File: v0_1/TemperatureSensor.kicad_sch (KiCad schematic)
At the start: 1 part, among them U3 AHT20

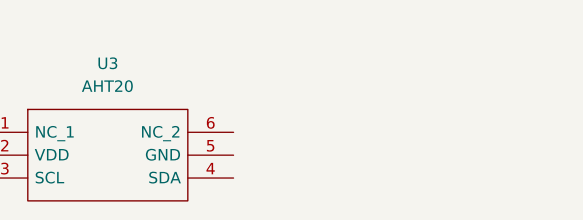
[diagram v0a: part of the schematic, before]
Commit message: add battery case
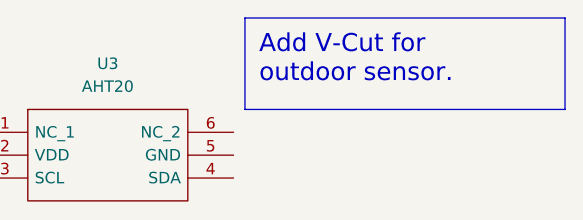
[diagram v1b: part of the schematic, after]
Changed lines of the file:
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@@
 (kicad_sch (version 20230121) (generator eeschema)
   (paper "A4")
+  (text_box "Add V-Cut for outdoor sensor.\n"
+    (at 128.27 67.31 0) (size 35.56 10.16)
+    (stroke (width 0) (type default))
+    (fill (type color) (color 235 255 31 1))
+    (effects (font (size 2 2)) (justify left top))
+  )
   (symbol (lib_id "AHT20:AHT20") (at 99.06 80.01 0) (unit 1)
     (in_bom yes) (on_board yes) (dnp no) (fields_autoplaced)

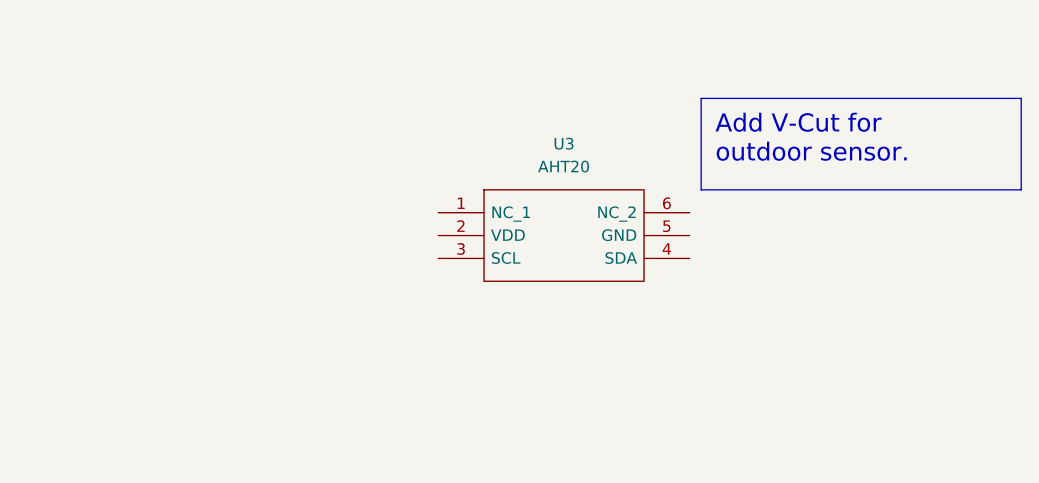
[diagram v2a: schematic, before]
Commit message: add rtc and charger schematic
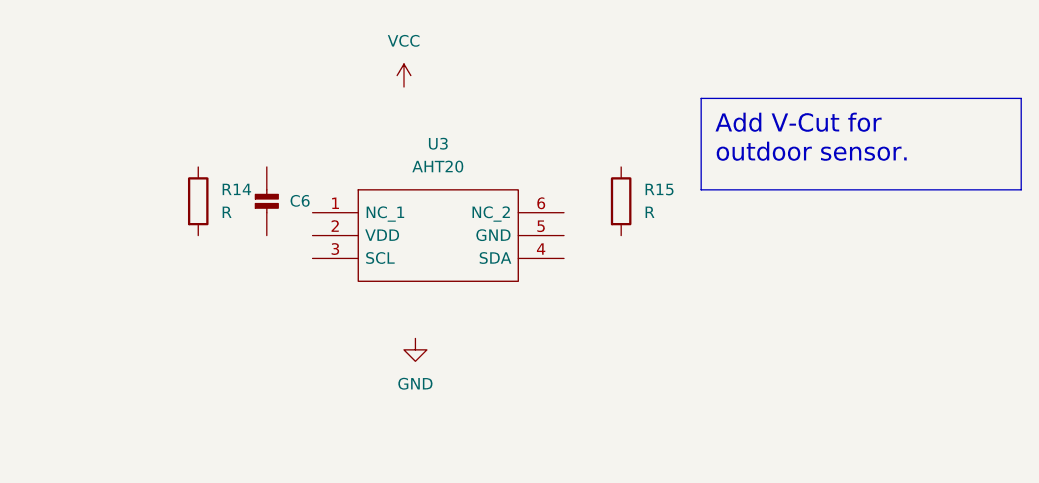
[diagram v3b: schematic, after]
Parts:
- added C6: ~, v0_1:_0603, symbol v0_1-eagle-import:CAP_CERAMIC_0603
- added R14, R15: R, symbol Device:R
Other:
- moved on the sheet: U3
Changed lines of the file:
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@@
     (effects (font (size 2 2)) (justify left top))
   )
-  (symbol (lib_id "AHT20:AHT20") (at 99.06 80.01 0) (unit 1)
+  (symbol (lib_id "AHT20:AHT20") (at 85.09 80.01 0) (unit 1)
     (in_bom yes) (on_board yes) (dnp no) (fields_autoplaced)
-    (property "Reference" "U3" (at 113.03 72.39 0)
+    (property "Reference" "U3" (at 99.06 72.39 0)
       (effects (font (size 1.27 1.27)))
     )
-    (property "Value" "AHT20" (at 113.03 74.93 0)
+    (property "Value" "AHT20" (at 99.06 74.93 0)
       (effects (font (size 1.27 1.27)))
     )
-    (property "Footprint" "AHT20:AHT20" (at 123.19 77.47 0)
+    (property "Footprint" "AHT20:AHT20" (at 109.22 77.47 0)
       (effects (font (size 1.27 1.27)) (justify left) hide)
     )
-    (property "Datasheet" "http://www.aosong.com/userfiles/files/media/Data%20Sheet%20AHT20.pdf" (at 123.19 80.01 0)
+    (property "Datasheet" "http://www.aosong.com/userfiles/files/media/Data%20Sheet%20AHT20.pdf" (at 109.22 80.01 0)
       (effects (font (size 1.27 1.27)) (justify left) hide)
     )
-    (property "Description" "Integrated temperature and humidity Sensor DC : 2.2 - 5.5V, 0 ~{} 100% RH, -40 ~{} + 85 ." (at 123.19 82.55 0)
+    (property "Description" "Integrated temperature and humidity Sensor DC : 2.2 - 5.5V, 0 ~{} 100% RH, -40 ~{} + 85 ." (at 109.22 82.55 0)
       (effects (font (size 1.27 1.27)) (justify left) hide)
     )
-    (property "Height" "1.1" (at 123.19 85.09 0)
+    (property "Height" "1.1" (at 109.22 85.09 0)
       (effects (font (size 1.27 1.27)) (justify left) hide)
     )
-    (property "Manufacturer_Name" "Aosong" (at 123.19 87.63 0)
+    (property "Manufacturer_Name" "Aosong" (at 109.22 87.63 0)
       (effects (font (size 1.27 1.27)) (justify left) hide)
     )
-    (property "Manufacturer_Part_Number" "AHT20" (at 123.19 90.17 0)
+    (property "Manufacturer_Part_Number" "AHT20" (at 109.22 90.17 0)
       (effects (font (size 1.27 1.27)) (justify left) hide)
     )
-    (property "Mouser Part Number" "" (at 123.19 92.71 0)
+    (property "Mouser Part Number" "" (at 109.22 92.71 0)
       (effects (font (size 1.27 1.27)) (justify left) hide)
     )
-    (property "Mouser Price/Stock" "" (at 123.19 95.25 0)
+    (property "Mouser Price/Stock" "" (at 109.22 95.25 0)
       (effects (font (size 1.27 1.27)) (justify left) hide)
     )
-    (property "Arrow Part Number" "" (at 123.19 97.79 0)
+    (property "Arrow Part Number" "" (at 109.22 97.79 0)
       (effects (font (size 1.27 1.27)) (justify left) hide)
     )
-    (property "Arrow Price/Stock" "" (at 123.19 100.33 0)
+    (property "Arrow Price/Stock" "" (at 109.22 100.33 0)
       (effects (font (size 1.27 1.27)) (justify left) hide)
     )
@@
         )
       )
+    )
+  )
+  (symbol (lib_id "power:GND") (at 96.52 93.98 0) (unit 1)
+    (in_bom yes) (on_board yes) (dnp no) (fields_autoplaced)
+    (property "Reference" "#PWR010" (at 96.52 100.33 0)
+      (effects (font (size 1.27 1.27)) hide)
+    )
+    (property "Value" "GND" (at 96.52 99.06 0)
+      (effects (font (size 1.27 1.27)))
+    )
+    (property "Footprint" "" (at 96.52 93.98 0)
+      (effects (font (size 1.27 1.27)) hide)
+    )
+    (property "Datasheet" "" (at 96.52 93.98 0)
+      (effects (font (size 1.27 1.27)) hide)
+    )
+    (pin "1")
+    (instances
+      (project "v0_1"
+        (path "/0bf090f4-b9b7-437f-9e6a-e818f47752ec/18c6dee4-287a-4eaf-8042-b3dc1f680c7d"
+          (reference "#PWR010") (unit 1)
+        )
+      )
+    )
+  )
+  (symbol (lib_id "power:VCC") (at 95.25 66.04 0) (unit 1)
+    (in_bom yes) (on_board yes) (dnp no) (fields_autoplaced)
+    (property "Reference" "#PWR09" (at 95.25 69.85 0)
+      (effects (font (size 1.27 1.27)) hide)
+    )
+    (property "Value" "VCC" (at 95.25 60.96 0)
+      (effects (font (size 1.27 1.27)))
+    )
+    (property "Footprint" "" (at 95.25 66.04 0)
+      (effects (font (size 1.27 1.27)) hide)
+    )
+    (property "Datasheet" "" (at 95.25 66.04 0)
+      (effects (font (size 1.27 1.27)) hide)
+    )
+    (pin "1")
+    (instances
+      (project "v0_1"
+        (path "/0bf090f4-b9b7-437f-9e6a-e818f47752ec/18c6dee4-287a-4eaf-8042-b3dc1f680c7d"
+          (reference "#PWR09") (unit 1)
+        )
+      )
+    )
+  )
+  (symbol (lib_id "v0_1-eagle-import:CAP_CERAMIC_0603") (at 80.01 80.01 0) (unit 1)
+    (in_bom yes) (on_board yes) (dnp no) (fields_autoplaced)
+    (property "Reference" "C6" (at 82.55 78.74 0)
+      (effects (font (size 1.27 1.27)) (justify left))
+    )
+    (property "Value" "~" (at 82.31 78.76 90)
+      (effects (font (size 1.27 1.27)))
+    )
+    (property "Footprint" "v0_1:_0603" (at 80.01 80.01 0)
+      (effects (font (size 1.27 1.27)) hide)
+    )
+    (property "Datasheet" "" (at 80.01 80.01 0)
+      (effects (font (size 1.27 1.27)) hide)
+    )
+    (pin "1")
+    (pin "2")
+    (instances
+      (project "v0_1"
+        (path "/0bf090f4-b9b7-437f-9e6a-e818f47752ec/18c6dee4-287a-4eaf-8042-b3dc1f680c7d"
+          (reference "C6") (unit 1)
+        )
+      )
+    )
+  )
+  (symbol (lib_id "Device:R") (at 119.38 78.74 0) (unit 1)
+    (in_bom yes) (on_board yes) (dnp no) (fields_autoplaced)
+    (property "Reference" "R15" (at 121.92 77.47 0)
+      (effects (font (size 1.27 1.27)) (justify left))
+    )
+    (property "Value" "R" (at 121.92 80.01 0)
+      (effects (font (size 1.27 1.27)) (justify left))
+    )
+    (property "Footprint" "" (at 117.602 78.74 90)
+      (effects (font (size 1.27 1.27)) hide)
+    )
+    (property "Datasheet" "~" (at 119.38 78.74 0)
+      (effects (font (size 1.27 1.27)) hide)
+    )
+    (pin "1")
+    (pin "2")
+    (instances
+      (project "v0_1"
+        (path "/0bf090f4-b9b7-437f-9e6a-e818f47752ec/18c6dee4-287a-4eaf-8042-b3dc1f680c7d"
+          (reference "R15") (unit 1)
+        )
+      )
+    )
+  )
+  (symbol (lib_id "Device:R") (at 72.39 78.74 0) (unit 1)
+    (in_bom yes) (on_board yes) (dnp no) (fields_autoplaced)
+    (property "Reference" "R14" (at 74.93 77.47 0)
+      (effects (font (size 1.27 1.27)) (justify left))
+    )
+    (property "Value" "R" (at 74.93 80.01 0)
+      (effects (font (size 1.27 1.27)) (justify left))
+    )
+    (property "Footprint" "" (at 70.612 78.74 90)
+      (effects (font (size 1.27 1.27)) hide)
+    )
+    (property "Datasheet" "~" (at 72.39 78.74 0)
+      (effects (font (size 1.27 1.27)) hide)
+    )
+    (pin "1")
+    (pin "2")
+    (instances
+      (project "v0_1"
+        (path "/0bf090f4-b9b7-437f-9e6a-e818f47752ec/18c6dee4-287a-4eaf-8042-b3dc1f680c7d"
+          (reference "R14") (unit 1)
+        )
+      )

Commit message: add 0.2V
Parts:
- C6: value ~ -> 10uF
- R14, R15: value R -> 10K
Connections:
- net GND: now also C6.2, U3.5 (GND)
- net +3.3V: now reaches U3.2 (VDD)
- net +3.3V: now also C6.1, R14.1, R15.1
- net SCL: now reaches U3.3 (SCL)
- net SCL: now also R14.2
- net SDA: now reaches U3.4 (SDA)
- net SDA: now also R15.2
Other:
- moved on the sheet: C6, R14, R15
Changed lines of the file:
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@@
 (kicad_sch (version 20230121) (generator eeschema)
   (paper "A4")
+  (junction (at 81.28 82.55) (diameter 0) (color 0 0 0 0)
+  )
+  (junction (at 76.2 67.31) (diameter 0) (color 0 0 0 0)
+  )
+  (junction (at 76.2 85.09) (diameter 0) (color 0 0 0 0)
+  )
+  (junction (at 68.58 88.9) (diameter 0) (color 0 0 0 0)
+  )
+  (junction (at 81.28 99.06) (diameter 0) (color 0 0 0 0)
+  )
+  (junction (at 68.58 67.31) (diameter 0) (color 0 0 0 0)
+  )
+  (wire (pts (xy 58.42 88.9) (xy 68.58 88.9))
+    (stroke (width 0) (type default))
+  )
+  (wire (pts (xy 76.2 67.31) (xy 81.28 67.31))
+    (stroke (width 0) (type default))
+  )
+  (wire (pts (xy 68.58 67.31) (xy 76.2 67.31))
+    (stroke (width 0) (type default))
+  )
+  (wire (pts (xy 81.28 82.55) (xy 81.28 67.31))
+    (stroke (width 0) (type default))
+  )
+  (wire (pts (xy 58.42 85.09) (xy 76.2 85.09))
+    (stroke (width 0) (type default))
+  )
+  (wire (pts (xy 113.03 82.55) (xy 116.84 82.55))
+    (stroke (width 0) (type default))
+  )
+  (wire (pts (xy 115.57 88.9) (xy 68.58 88.9))
+    (stroke (width 0) (type default))
+  )
+  (wire (pts (xy 76.2 83.82) (xy 76.2 85.09))
+    (stroke (width 0) (type default))
+  )
+  (wire (pts (xy 68.58 76.2) (xy 68.58 67.31))
+    (stroke (width 0) (type default))
+  )
+  (wire (pts (xy 81.28 82.55) (xy 81.28 90.17))
+    (stroke (width 0) (type default))
+  )
+  (wire (pts (xy 116.84 82.55) (xy 116.84 99.06))
+    (stroke (width 0) (type default))
+  )
+  (wire (pts (xy 115.57 85.09) (xy 115.57 88.9))
+    (stroke (width 0) (type default))
+  )
+  (wire (pts (xy 81.28 97.79) (xy 81.28 99.06))
+    (stroke (width 0) (type default))
+  )
+  (wire (pts (xy 81.28 99.06) (xy 116.84 99.06))
+    (stroke (width 0) (type default))
+  )
+  (wire (pts (xy 81.28 99.06) (xy 81.28 101.6))
+    (stroke (width 0) (type default))
+  )
+  (wire (pts (xy 76.2 85.09) (xy 85.09 85.09))
+    (stroke (width 0) (type default))
+  )
+  (wire (pts (xy 113.03 85.09) (xy 115.57 85.09))
+    (stroke (width 0) (type default))
+  )
+  (wire (pts (xy 68.58 64.77) (xy 68.58 67.31))
+    (stroke (width 0) (type default))
+  )
+  (wire (pts (xy 81.28 82.55) (xy 85.09 82.55))
+    (stroke (width 0) (type default))
+  )
+  (wire (pts (xy 76.2 76.2) (xy 76.2 67.31))
+    (stroke (width 0) (type default))
+  )
+  (wire (pts (xy 68.58 88.9) (xy 68.58 83.82))
+    (stroke (width 0) (type default))
+  )
   (text_box "Add V-Cut for outdoor sensor.\n"
     (at 128.27 67.31 0) (size 35.56 10.16)
@@
     (fill (type color) (color 235 255 31 1))
     (effects (font (size 2 2)) (justify left top))
+  )
+  (hierarchical_label "SCL" (shape input) (at 58.42 85.09 180) (fields_autoplaced)
+    (effects (font (size 1.27 1.27)) (justify right))
+  )
+  (hierarchical_label "SDA" (shape input) (at 58.42 88.9 180) (fields_autoplaced)
+    (effects (font (size 1.27 1.27)) (justify right))
+  )
+  (symbol (lib_id "power:+3.3V") (at 68.58 64.77 0) (unit 1)
+    (in_bom yes) (on_board yes) (dnp no) (fields_autoplaced)
+    (property "Reference" "#PWR09" (at 68.58 68.58 0)
+      (effects (font (size 1.27 1.27)) hide)
+    )
+    (property "Value" "+3.3V" (at 68.58 59.69 0)
+      (effects (font (size 1.27 1.27)))
+    )
+    (property "Footprint" "" (at 68.58 64.77 0)
+      (effects (font (size 1.27 1.27)) hide)
+    )
+    (property "Datasheet" "" (at 68.58 64.77 0)
+      (effects (font (size 1.27 1.27)) hide)
+    )
+    (pin "1")
+    (instances
+      (project "v0_1"
+        (path "/0bf090f4-b9b7-437f-9e6a-e818f47752ec/18c6dee4-287a-4eaf-8042-b3dc1f680c7d"
+          (reference "#PWR09") (unit 1)
+        )
+      )
+    )
   )
   (symbol (lib_id "AHT20:AHT20") (at 85.09 80.01 0) (unit 1)
@@
     )
   )
-  (symbol (lib_id "power:GND") (at 96.52 93.98 0) (unit 1)
-    (in_bom yes) (on_board yes) (dnp no) (fields_autoplaced)
-    (property "Reference" "#PWR010" (at 96.52 100.33 0)
-      (effects (font (size 1.27 1.27)) hide)
-    )
-    (property "Value" "GND" (at 96.52 99.06 0)
-      (effects (font (size 1.27 1.27)))
-    )
-    (property "Footprint" "" (at 96.52 93.98 0)
-      (effects (font (size 1.27 1.27)) hide)
-    )
-    (property "Datasheet" "" (at 96.52 93.98 0)
+  (symbol (lib_id "power:GND") (at 81.28 101.6 0) (unit 1)
+    (in_bom yes) (on_board yes) (dnp no) (fields_autoplaced)
+    (property "Reference" "#PWR010" (at 81.28 107.95 0)
+      (effects (font (size 1.27 1.27)) hide)
+    )
+    (property "Value" "GND" (at 81.28 106.68 0)
+      (effects (font (size 1.27 1.27)))
+    )
+    (property "Footprint" "" (at 81.28 101.6 0)
+      (effects (font (size 1.27 1.27)) hide)
+    )
+    (property "Datasheet" "" (at 81.28 101.6 0)
       (effects (font (size 1.27 1.27)) hide)
     )
@@
     )
   )
-  (symbol (lib_id "power:VCC") (at 95.25 66.04 0) (unit 1)
-    (in_bom yes) (on_board yes) (dnp no) (fields_autoplaced)
-    (property "Reference" "#PWR09" (at 95.25 69.85 0)
-      (effects (font (size 1.27 1.27)) hide)
-    )
-    (property "Value" "VCC" (at 95.25 60.96 0)
-      (effects (font (size 1.27 1.27)))
-    )
-    (property "Footprint" "" (at 95.25 66.04 0)
-      (effects (font (size 1.27 1.27)) hide)
-    )
-    (property "Datasheet" "" (at 95.25 66.04 0)
-      (effects (font (size 1.27 1.27)) hide)
-    )
-    (pin "1")
-    (instances
-      (project "v0_1"
-        (path "/0bf090f4-b9b7-437f-9e6a-e818f47752ec/18c6dee4-287a-4eaf-8042-b3dc1f680c7d"
-          (reference "#PWR09") (unit 1)
-        )
-      )
-    )
-  )
-  (symbol (lib_id "v0_1-eagle-import:CAP_CERAMIC_0603") (at 80.01 80.01 0) (unit 1)
-    (in_bom yes) (on_board yes) (dnp no) (fields_autoplaced)
-    (property "Reference" "C6" (at 82.55 78.74 0)
-      (effects (font (size 1.27 1.27)) (justify left))
-    )
-    (property "Value" "~" (at 82.31 78.76 90)
-      (effects (font (size 1.27 1.27)))
-    )
-    (property "Footprint" "v0_1:_0603" (at 80.01 80.01 0)
-      (effects (font (size 1.27 1.27)) hide)
-    )
-    (property "Datasheet" "" (at 80.01 80.01 0)
+  (symbol (lib_id "v0_1-eagle-import:CAP_CERAMIC_0603") (at 81.28 95.25 0) (unit 1)
+    (in_bom yes) (on_board yes) (dnp no) (fields_autoplaced)
+    (property "Reference" "C6" (at 83.82 93.98 0)
+      (effects (font (size 1.27 1.27)) (justify left))
+    )
+    (property "Value" "10uF" (at 83.58 94 90)
+      (effects (font (size 1.27 1.27)))
+    )
+    (property "Footprint" "v0_1:_0603" (at 81.28 95.25 0)
+      (effects (font (size 1.27 1.27)) hide)
+    )
+    (property "Datasheet" "" (at 81.28 95.25 0)
       (effects (font (size 1.27 1.27)) hide)
     )
@@
     )
   )
-  (symbol (lib_id "Device:R") (at 119.38 78.74 0) (unit 1)
-    (in_bom yes) (on_board yes) (dnp no) (fields_autoplaced)
-    (property "Reference" "R15" (at 121.92 77.47 0)
-      (effects (font (size 1.27 1.27)) (justify left))
-    )
-    (property "Value" "R" (at 121.92 80.01 0)
-      (effects (font (size 1.27 1.27)) (justify left))
-    )
-    (property "Footprint" "" (at 117.602 78.74 90)
-      (effects (font (size 1.27 1.27)) hide)
-    )
-    (property "Datasheet" "~" (at 119.38 78.74 0)
+  (symbol (lib_id "Device:R") (at 68.58 80.01 0) (unit 1)
+    (in_bom yes) (on_board yes) (dnp no) (fields_autoplaced)
+    (property "Reference" "R15" (at 71.12 78.74 0)
+      (effects (font (size 1.27 1.27)) (justify left))
+    )
+    (property "Value" "10K" (at 71.12 81.28 0)
+      (effects (font (size 1.27 1.27)) (justify left))
+    )
+    (property "Footprint" "" (at 66.802 80.01 90)
+      (effects (font (size 1.27 1.27)) hide)
+    )
+    (property "Datasheet" "~" (at 68.58 80.01 0)
       (effects (font (size 1.27 1.27)) hide)
     )
@@
     )
   )
-  (symbol (lib_id "Device:R") (at 72.39 78.74 0) (unit 1)
-    (in_bom yes) (on_board yes) (dnp no) (fields_autoplaced)
-    (property "Reference" "R14" (at 74.93 77.47 0)
-      (effects (font (size 1.27 1.27)) (justify left))
-    )
-    (property "Value" "R" (at 74.93 80.01 0)
-      (effects (font (size 1.27 1.27)) (justify left))
-    )
-    (property "Footprint" "" (at 70.612 78.74 90)
-      (effects (font (size 1.27 1.27)) hide)
-    )
-    (property "Datasheet" "~" (at 72.39 78.74 0)
-      (effects (font (size 1.27 1.27)) hide)
-    )
+  (symbol (lib_id "Device:R") (at 76.2 80.01 0) (unit 1)
+    (in_bom yes) (on_board yes) (dnp no) (fields_autoplaced)
+    (property "Reference" "R14" (at 78.74 78.74 0)
+      (effects (font (size 1.27 1.27)) (justify left))
+    )
+    (property "Value" "10K" (at 78.74 81.28 0)
+      (effects (font (size 1.27 1.27)) (justify left))
+    )
+    (property "Footprint" "" (at 74.422 80.01 90)
+      (effects (font (size 1.27 1.27)) hide)
+    )
+    (property "Datasheet" "~" (at 76.2 80.01 0)
+      (effects (font (size 1.27 1.27)) hide)
+    )
